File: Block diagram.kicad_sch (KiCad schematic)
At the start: 0 parts

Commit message: Refactoring sch
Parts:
- added H701, H702, H703, H704, H705, H706, H707, H708: MountingHole, MountingHole:MountingHole_3.2mm_M3, symbol Mechanical:MountingHole
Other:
- added sheet HMI (HMI.kicad_sch)
- note removed: ">> NORMAL >> OPERATION"
- note removed: "Time [ms]"
- note removed: "Voltage [V]"
- title: Power - Sequencing -> Project Architecture

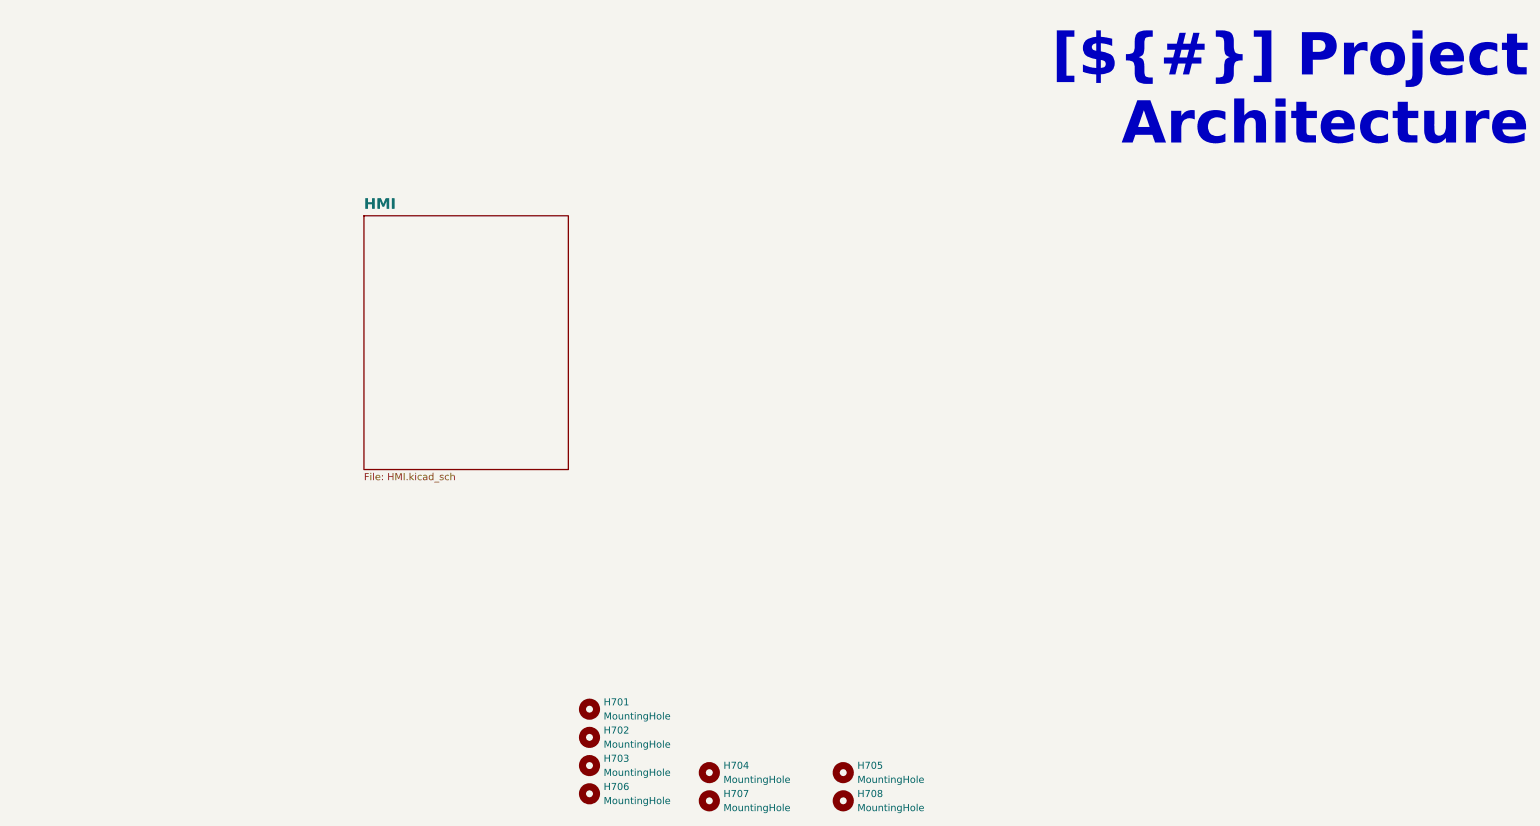
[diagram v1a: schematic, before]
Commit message: sch refactoring complete
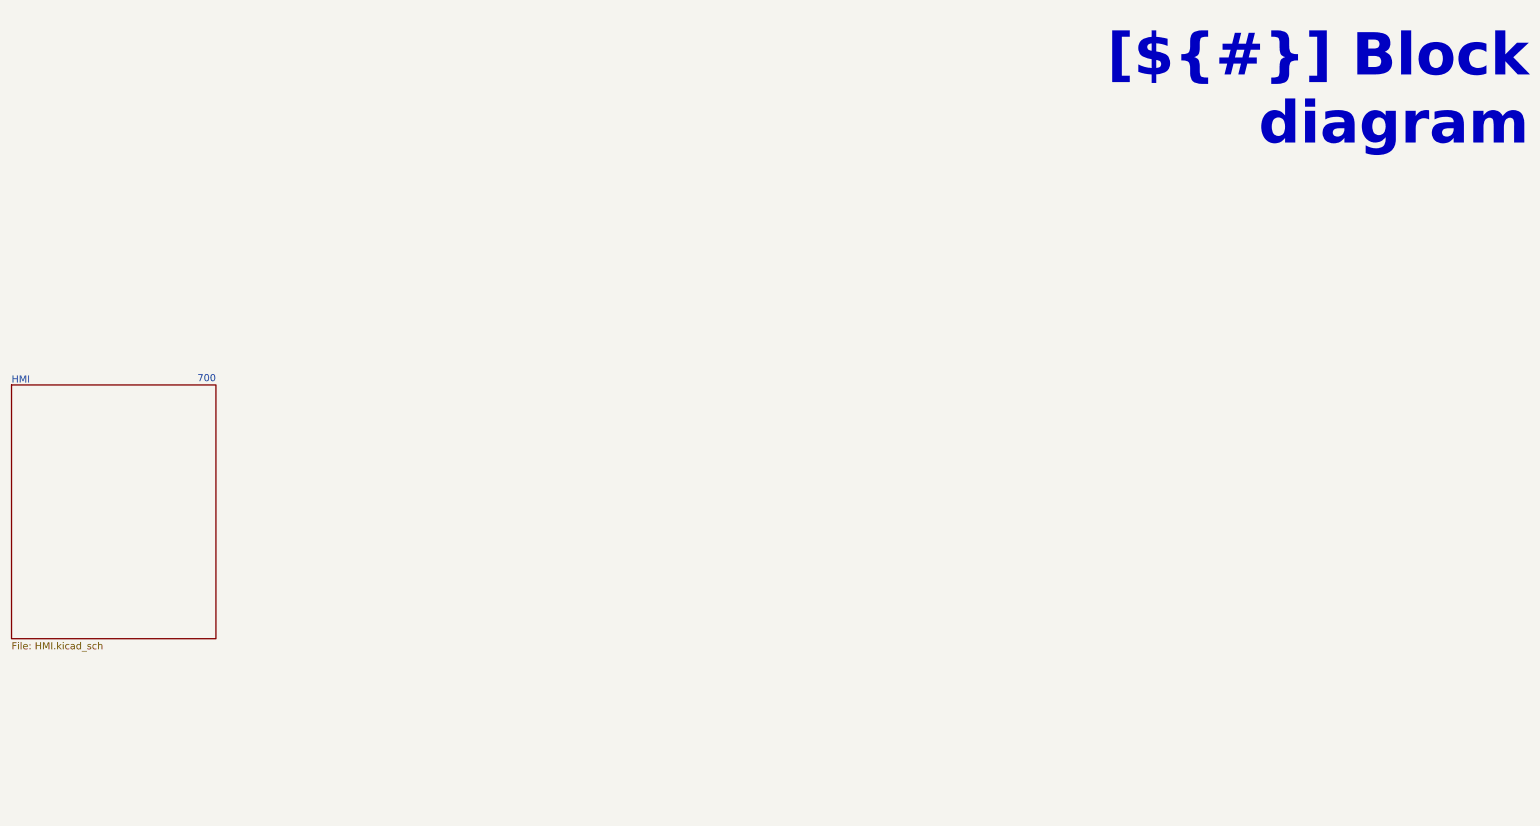
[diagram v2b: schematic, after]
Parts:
- removed H701, H702, H703, H704, H705, H706, H707, H708: MountingHole, MountingHole:MountingHole_3.2mm_M3, symbol Mechanical:MountingHole
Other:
- title: Project Architecture -> Block diagram

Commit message: Added code, pictures, readme, updated sch size and notes, changed to checked
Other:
- note added: "Interim solution 1"
- note added: "Interim solution 2"
- note added: "Main board"
- note added: "Power supply"
- note added: "Repo link"
- note added: "Scope of this document"
- note added: "Separate repositories"
- note added: "Under development"
